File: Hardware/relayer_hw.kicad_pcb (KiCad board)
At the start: 4 copper layers, 40 x 80 mm, 57 parts, among them J1 BOOT0, J2 AC_OUT, J3 STLink, J4 AC_IN, Q1 2N7002, SW1 NRST, SW2 USR_SW, U1 STM32WB55, U2 902-9040, U3 LM1117-3.3, Y1 Crystal, Y2 Crystal_GND23

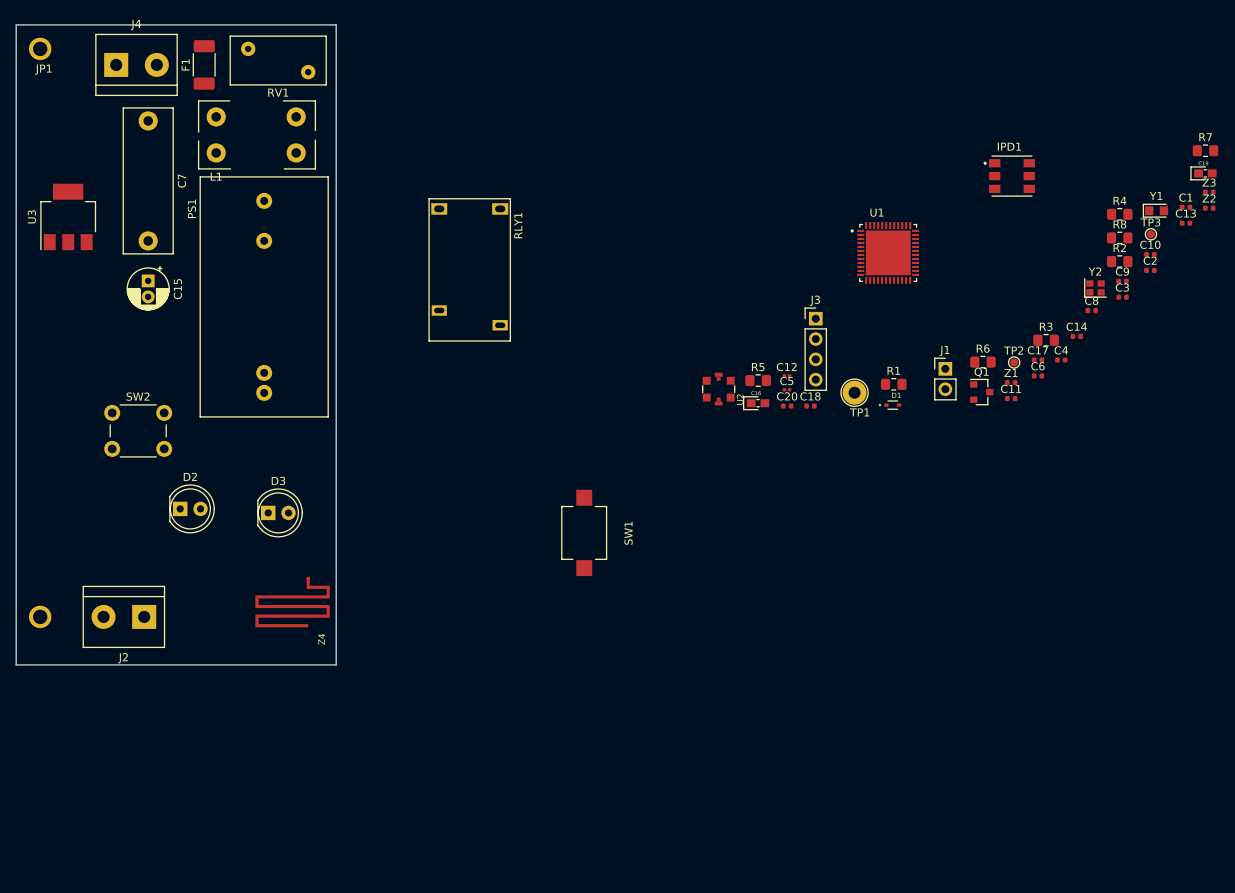
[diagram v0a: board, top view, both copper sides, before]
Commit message: Correção nos cristais/Posicionamento dos componentes em andamento
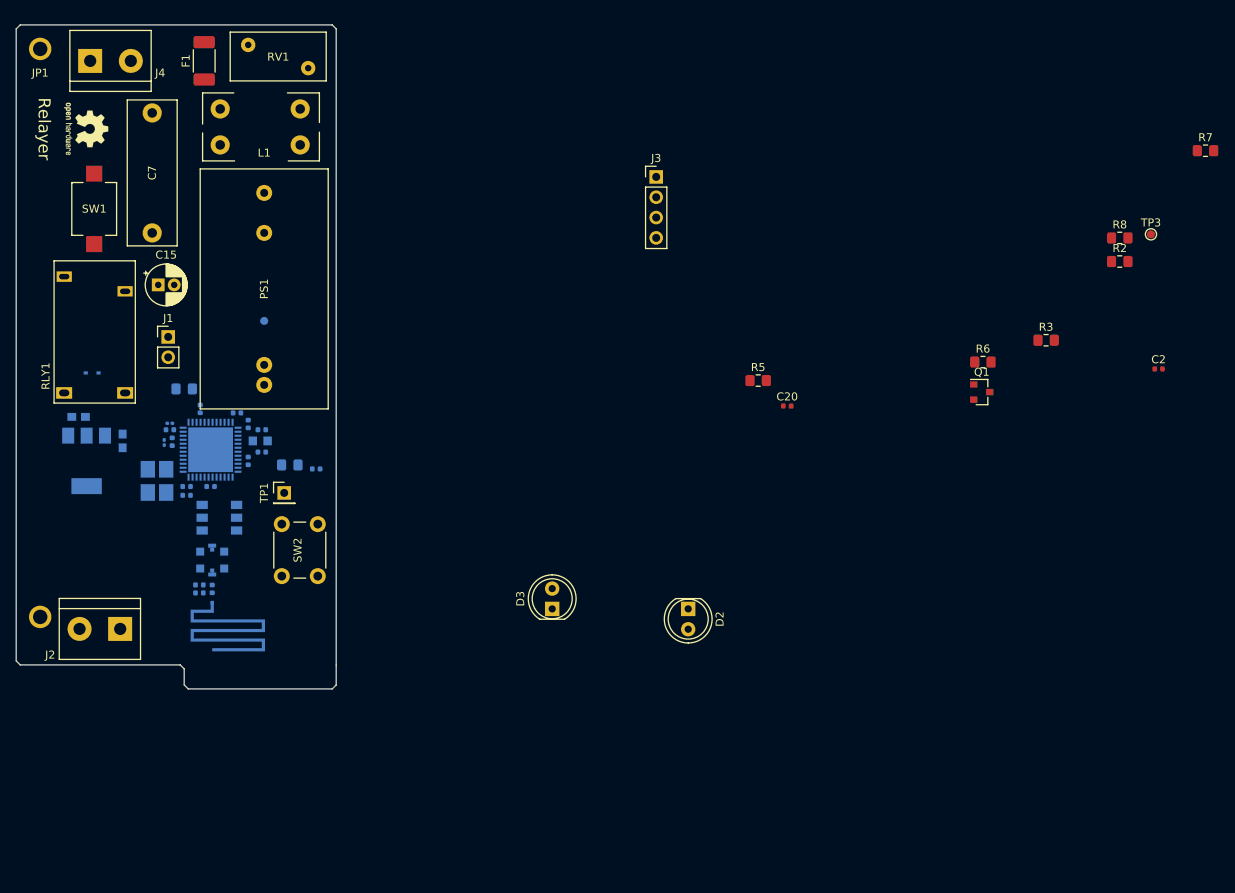
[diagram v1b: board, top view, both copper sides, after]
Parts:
- added REF**: OSHW-Logo2_7.3x6mm_SilkScreen, Symbol:OSHW-Logo2_7.3x6mm_SilkScreen, F.Cu at (53.8, 48.0)
- C1, C4: value 10pF -> 12pF; moved to B.Cu
- C10, C11, C12, C13, C14, C16, C17, C18, C19, C3, C5, C6, C8, C9, D1, IPD1, R1, R4, TP2, U1, U2, U3, Z1, Z2, Z3, Z4: moved to B.Cu
- F1: footprint Fuse:Fuse_2010_5025Metric_Pad1.52x2.65mm_HandSolder -> Usr_pretty_lib:Fuse_2010_5025Metric_Pad1.52x2.65mm_HandSolder
- J2: footprint TerminalBlock:TerminalBlock_bornier-2_P5.08mm -> Usr_pretty_lib:TerminalBlock_bornier-2_P5.08mm
- TP1: footprint TestPoint:TestPoint_Loop_D2.54mm_Drill1.5mm_Beaded -> Connector_PinHeader_2.54mm:PinHeader_1x01_P2.54mm_Vertical
- Y1: footprint Crystal:Crystal_SMD_2012-2Pin_2.0x1.2mm_HandSoldering -> Usr_pretty_lib:Crystal_SMD_2012-2Pin_2.0x1.2mm_HandSoldering; moved to B.Cu
- Y2: footprint Crystal:Crystal_SMD_2016-4Pin_2.0x1.6mm -> Usr_pretty_lib:Crystal_SMD_3225-4Pin_3.2x2.5mm_HandSoldering; moved to B.Cu
- moved C19 144.1 mm to (52.8, 84.0), turned to 180 degrees
- moved Z3 135.8 mm to (67.9, 106.0), turned to 180 degrees
- moved Z2 133.4 mm to (69.5, 105.5), turned to 90 degrees
- moved C13 125.4 mm to (68.0, 83.0), turned to 90 degrees
- moved C10 121.0 mm to (69.3, 92.7)
- moved Y2 119.8 mm to (62.6, 92.0), turned to 90 degrees
- moved C1 118.8 mm to (75.7, 85.6), turned to 180 degrees
- moved Y1 115.7 mm to (75.5, 87.0), turned to 180 degrees
- moved C14 113.8 mm to (64.5, 87.1), turned to 270 degrees
- moved C9 111.6 mm to (74.0, 89.5), turned to 270 degrees
- moved C6 108.7 mm to (64.2, 85.6), turned to 180 degrees
- moved R4 108.4 mm to (79.2, 90.0)
- moved IPD1 107.9 mm to (70.4, 96.6)
- moved C17 107.8 mm to (66.3, 93.8), turned to 180 degrees
- moved C8 107.6 mm to (72.6, 83.5)
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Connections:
- J1 pad 1: Net-(J1-Pad1) -> 3V3
- J2 pad 1: N -> Net-(J2-Pad1)
- J2 pad 2: Net-(J2-Pad2) -> N
- J3 pad 2: Net-(J3-Pad2) -> 3V3
- RLY1 pad AC1: F -> F_IN
- RLY1 pad AC2: Net-(J2-Pad2) -> Net-(J2-Pad1)
- U1 pad 12: Net-(U1-Pad12) -> Net-(R4-Pad1)
- U1 pad 22: Net-(U1-Pad22) -> GND
- U1 pad 9: Net-(R4-Pad1) -> Net-(U1-Pad9)
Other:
- board size 40 x 80 mm -> 40 x 83 mm
- net class AC_default added: clearance 0.8, trace_width 0.5, via_dia 0.6, via_drill 0.3
- net class AC_high_power added: clearance 2.5, trace_width 1.5, via_dia 0.8, via_drill 0.4
- net class Default: via_dia 0.8 -> 0.6; via_drill 0.4 -> 0.3
- net class RF_trace added: clearance 0.2, trace_width 0.25, via_dia 0.6, via_drill 0.3
- board text added: "Relayer"

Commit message: Rotas dos caps de desacoplamento/ zonas de cobre externas/ posicionamento de componentes
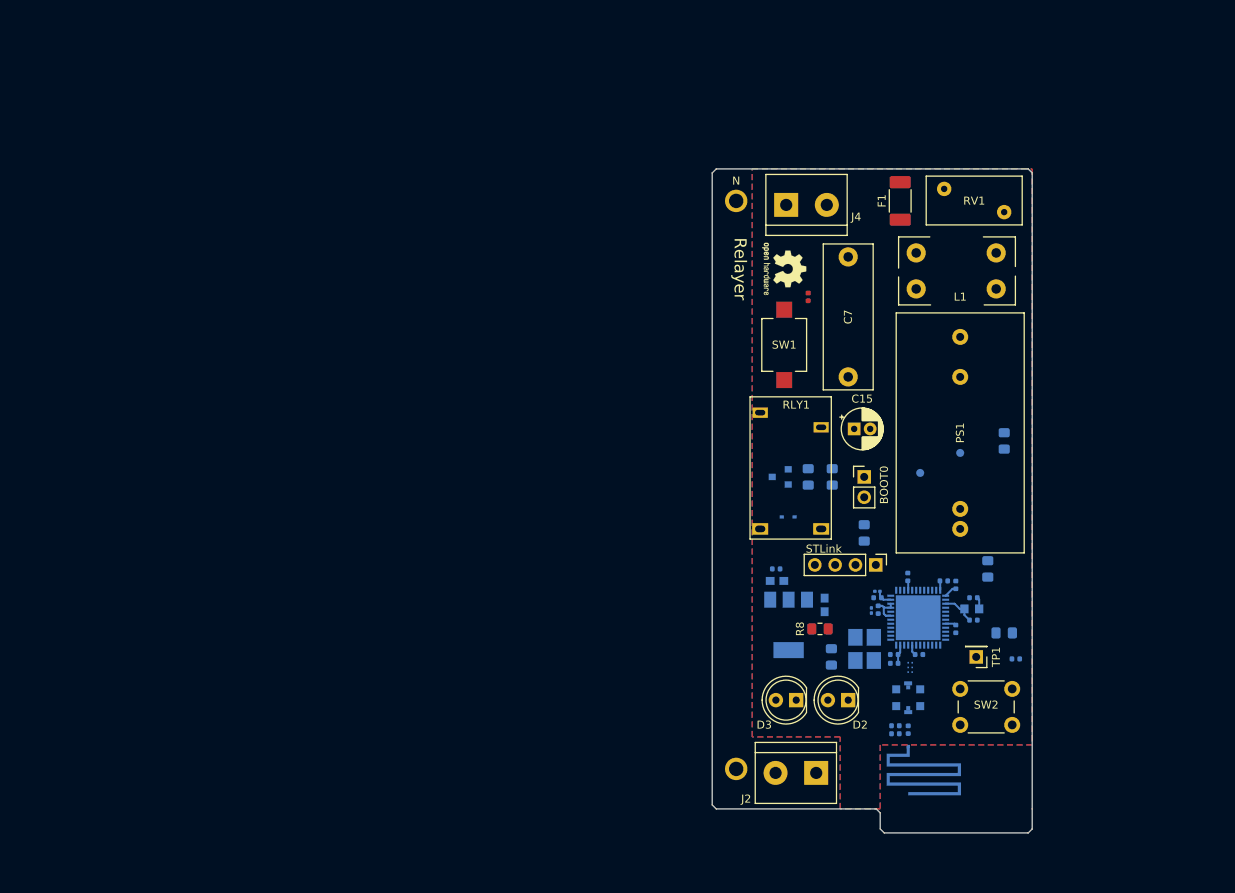
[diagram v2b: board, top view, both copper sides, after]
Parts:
- removed J1: BOOT0, Connector_PinHeader_2.54mm:PinHeader_1x02_P2.54mm_Vertical
- removed J3: STLink, Connector_PinHeader_2.54mm:PinHeader_1x04_P2.54mm_Vertical
- removed JP1: Wire, Usr_pretty_lib:neutral_wire
- added BOOT0: BOOT0, Connector_PinHeader_2.54mm:PinHeader_1x02_P2.54mm_Vertical, F.Cu at (151.0, 91.5)
- added N: Wire, Usr_pretty_lib:neutral_wire, F.Cu at (135.0, 55.0)
- added STLink: STLink, Connector_PinHeader_2.54mm:PinHeader_1x04_P2.54mm_Vertical, F.Cu at (152.4, 102.5)
- C20, Q1, R2, R3, R5, R6, R7, TP3: moved to B.Cu
- IPD1: footprint Usr_pretty_lib:SON160P500X500X140-6N -> Usr_pretty_lib:MLPF-WB55-01E3
- moved R4 91.7 mm to (168.5, 111.0)
- moved C1 91.4 mm to (164.7, 106.6)
- moved C4 91.4 mm to (164.7, 109.4)
- moved Y1 91.4 mm to (164.4, 108.0)
- moved C10 91.0 mm to (157.8, 113.7)
- moved Y2 90.9 mm to (151.1, 113.0)
- moved C17 90.9 mm to (154.8, 114.8)
- moved C18 90.9 mm to (154.8, 113.7)
- moved C5 90.9 mm to (152.7, 105.8)
- moved U1 90.9 mm to (157.8, 109.1)
- moved C13 90.9 mm to (156.4, 104.0)
- moved C6 90.9 mm to (152.7, 106.6)
- moved C9 90.9 mm to (162.4, 110.5)
- moved C12 90.9 mm to (151.9, 108.2)
- moved C8 90.8 mm to (160.9, 104.5)
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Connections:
- U1 pad 29: Net-(U1-Pad29) -> Net-(R7-Pad1)
- U1 pad 30: Net-(U1-Pad30) -> Net-(R8-Pad1)
- U1 pad 36: Net-(R8-Pad1) -> Net-(U1-Pad36)
- U1 pad 37: Net-(R7-Pad1) -> Net-(U1-Pad37)
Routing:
- net 3V3: track 0.00 -> 15.2 mm
- net Net-(C4-Pad1): track 0.00 -> 4.28 mm
- net Net-(C1-Pad1): track 0.00 -> 1.50 mm
- added copper zone on B.Cu, net GND
- added copper zone on F.Cu, net GND

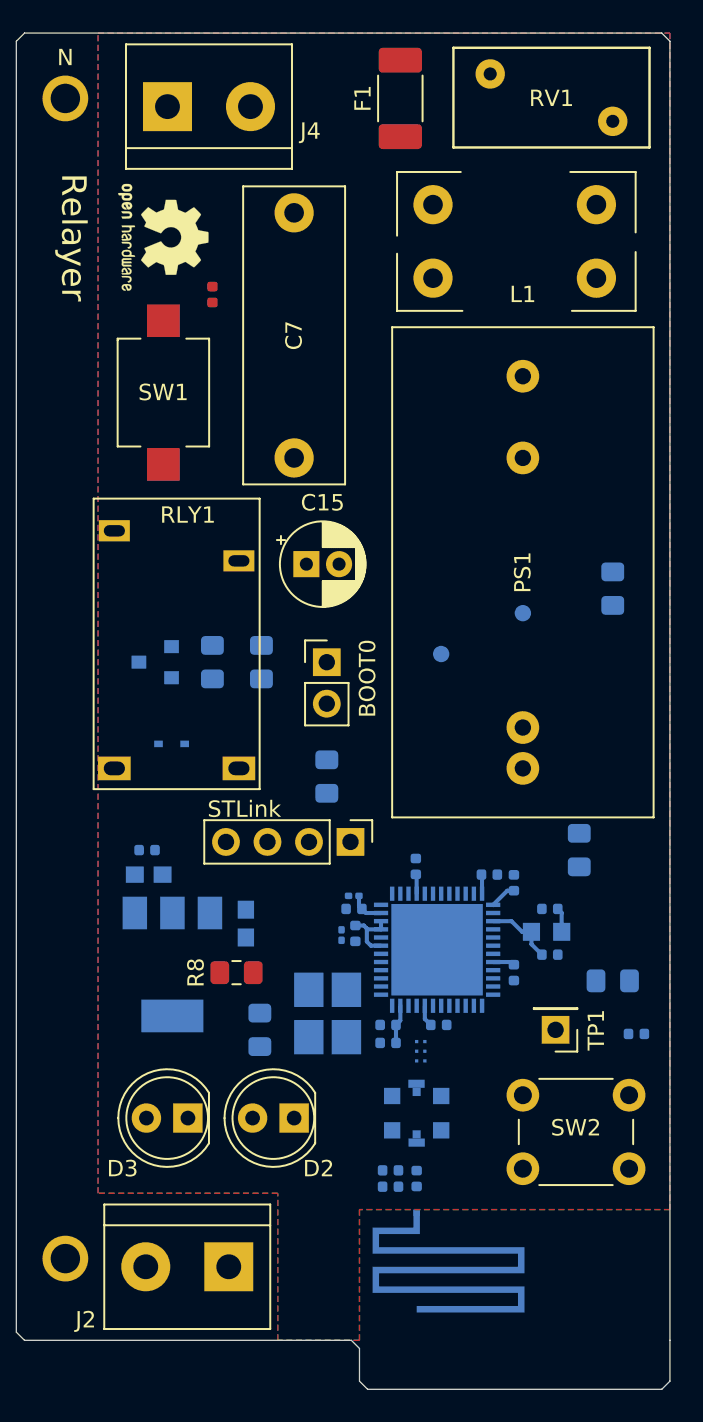
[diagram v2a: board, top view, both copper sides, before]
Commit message: Ajustes nos caps de desacoplamento/ Primeiras rotas
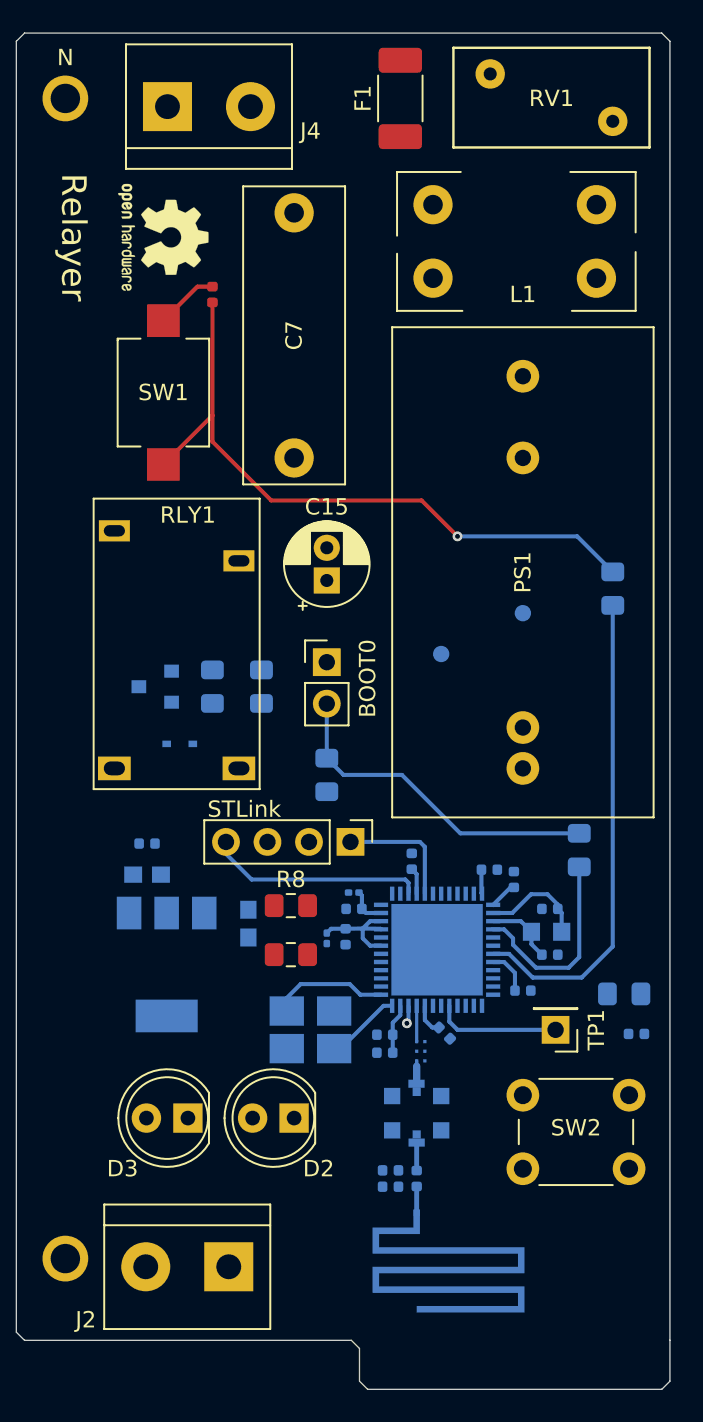
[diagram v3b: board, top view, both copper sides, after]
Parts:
- R7: moved to F.Cu
- moved R8 5.28 mm to (148.8, 106.4)
- moved R7 4.98 mm to (148.8, 109.4), turned to 180 degrees
- moved C15 1.60 mm to (151.0, 86.5), turned to 90 degrees
- moved Q1 1.50 mm to (140.5, 93.0)
- moved R5 1.50 mm to (144.0, 93.0)
- moved R6 1.50 mm to (147.0, 93.0)
- moved Y2 1.45 mm to (150.0, 114.0), turned to 180 degrees
- moved C9 1.23 mm to (163.0, 111.6), turned to 0 degrees
- moved R4 1.06 mm to (169.2, 111.8)
- moved C12 0.92 mm to (151.0, 108.4)
- moved C17 0.63 mm to (154.6, 115.4)
- moved C14 0.63 mm to (152.2, 108.3)
- moved C18 0.63 mm to (154.6, 114.3)
- moved C10 0.61 mm to (158.2, 114.2), turned to 315 degrees
- moved D1 0.50 mm to (142.0, 96.5)
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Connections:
- U3 pad 4: (no net) -> 3V3
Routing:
- net Net-(C2-Pad2): track 0.00 -> 40.6 mm, vias 0 -> 1
- net Net-(R3-Pad1): track 0.00 -> 29.6 mm
- net Net-(J1-Pad2): track 0.00 -> 20.7 mm
- net Net-(J3-Pad4): track 0.00 -> 13.8 mm
- net Net-(R2-Pad1): track 0.00 -> 12.3 mm
- net Net-(TP1-Pad1): track 0.00 -> 7.68 mm
- net Net-(J3-Pad1): track 0.00 -> 7.54 mm
- net Net-(U1-Pad25): track 0.00 -> 7.19 mm
- net 3V3: track 15.2 -> 21.8 mm
- net GND: track 0.00 -> 5.19 mm, vias 0 -> 1
- net Net-(C1-Pad1): track 1.50 -> 6.46 mm
- net Net-(U1-Pad24): track 0.00 -> 4.64 mm
- net Net-(IPD1-Pad3): track 0.00 -> 2.19 mm
- net Net-(U2-Pad2): track 0.00 -> 1.71 mm
- net Net-(Z2-Pad1): track 0.00 -> 1.62 mm
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- removed copper zone on B.Cu, net GND
- removed copper zone on F.Cu, net GND
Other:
- net class RF_trace: trace_width 0.25 -> 0.29

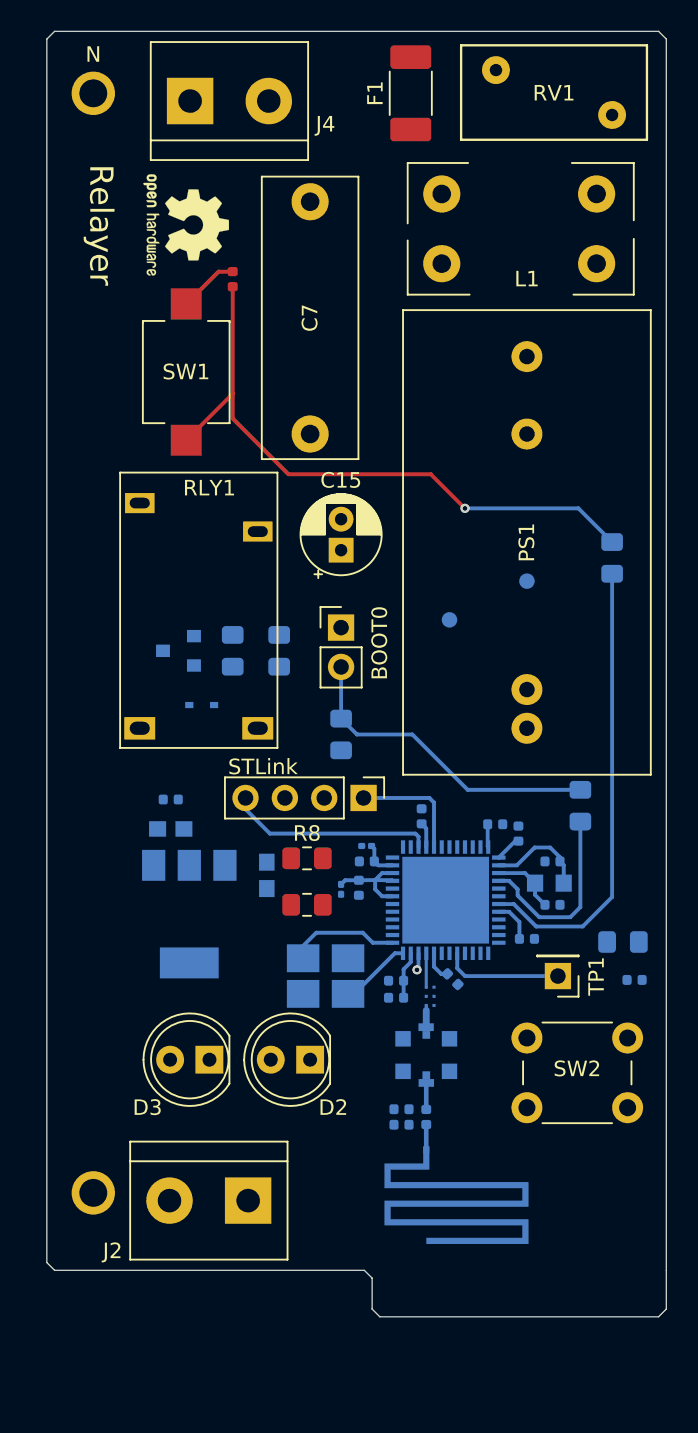
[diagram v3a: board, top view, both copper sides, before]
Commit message: Tamanho ajustado para caixa IP67 e rotas completas
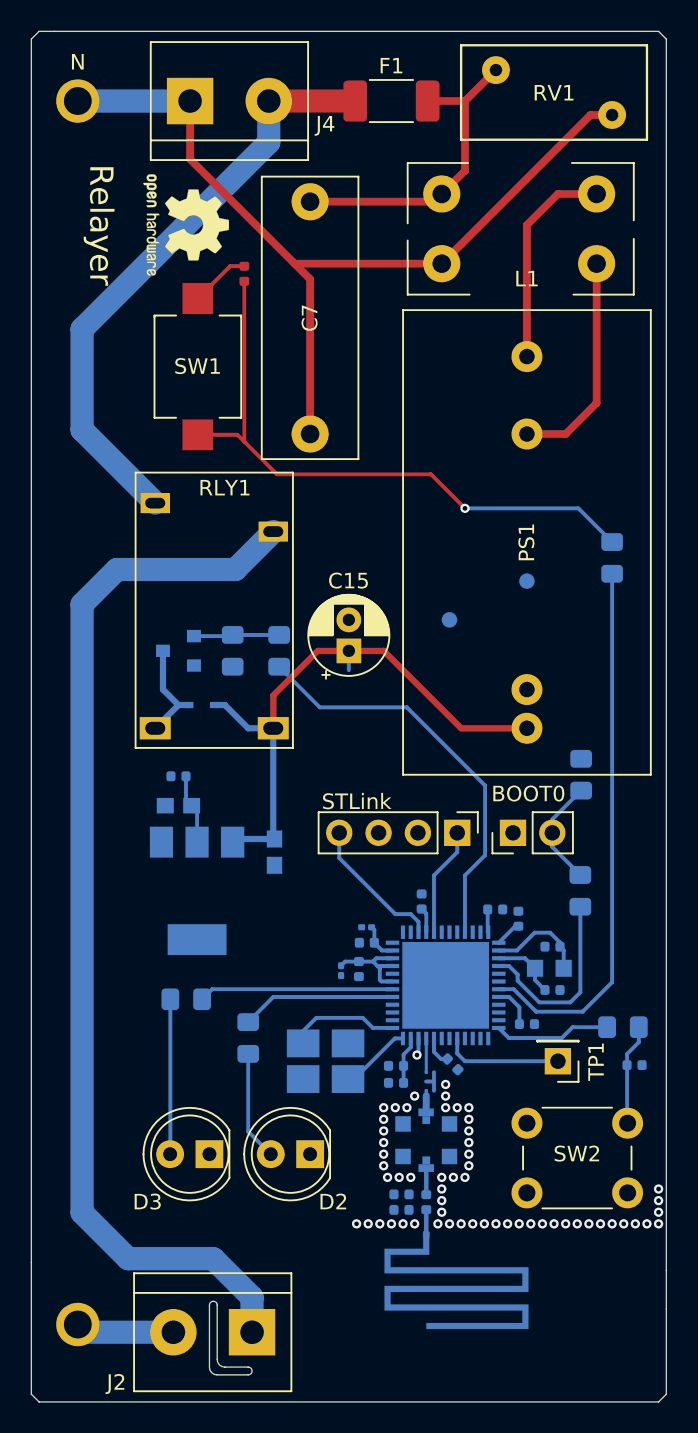
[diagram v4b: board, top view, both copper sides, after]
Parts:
- R7, R8: moved to B.Cu
- moved BOOT0 17.3 mm to (162.1, 104.8), turned to 90 degrees
- moved R1 15.7 mm to (166.5, 101.0), turned to 90 degrees
- moved R8 12.0 mm to (141.0, 115.5)
- moved R7 9.40 mm to (145.0, 118.0), turned to 270 degrees
- moved J2 8.50 mm to (145.2, 137.0)
- moved C15 6.52 mm to (151.5, 93.0)
- moved STLink 6.45 mm to (158.5, 104.8)
- moved D2 6.10 mm to (149.0, 125.5)
- moved D3 6.10 mm to (142.5, 125.5)
- moved C1 5.50 mm to (164.7, 112.1)
- moved C10 5.50 mm to (158.2, 119.7)
- moved C11 5.50 mm to (162.4, 110.3)
- moved C13 5.50 mm to (156.2, 109.2)
- moved C17 5.50 mm to (154.6, 120.9)
- moved C18 5.50 mm to (154.6, 119.8)
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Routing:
- net Net-(J2-Pad1): track 0.00 -> 69.1 mm
- net N: track 0.00 -> 62.8 mm
- net F_IN: track 0.00 -> 38.5 mm
- net 5V: track 0.00 -> 37.4 mm
- net Net-(R6-Pad1): track 0.00 -> 26.5 mm
- net F: track 0.00 -> 21.1 mm
- net Net-(L1-Pad3): track 0.00 -> 14.3 mm
- net Net-(L1-Pad4): track 0.00 -> 13.8 mm
- net Net-(J1-Pad2): track 20.7 -> 6.97 mm
- net Net-(R8-Pad1): track 0.00 -> 12.6 mm
- net Net-(D3-Pad2): track 0.00 -> 10.0 mm
- net Net-(R7-Pad1): track 0.00 -> 9.99 mm
- net Net-(R4-Pad1): track 0.00 -> 7.55 mm
- net Net-(D2-Pad2): track 0.00 -> 7.08 mm
- net Net-(D1-Pad2): track 0.00 -> 6.74 mm
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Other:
- board size 40 x 83 mm -> 41 x 88.5 mm
- net class DC_power added: clearance 0.2, trace_width 0.4, via_dia 0.6, via_drill 0.3
